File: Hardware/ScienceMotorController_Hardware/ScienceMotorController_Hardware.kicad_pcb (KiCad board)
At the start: 2 copper layers, 124.5 x 104.9 mm, 105 parts, among them SW1 SW_Push, SW2 SW_Push, SW3 SW_Push, SW4 SW_Push, SW5 SW_Push, U1 TM4C129E_Launchpad, U2 3.3V OKI, U3 5V OKI, U4 VNH5019A_E, U5 VNH5019A_E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

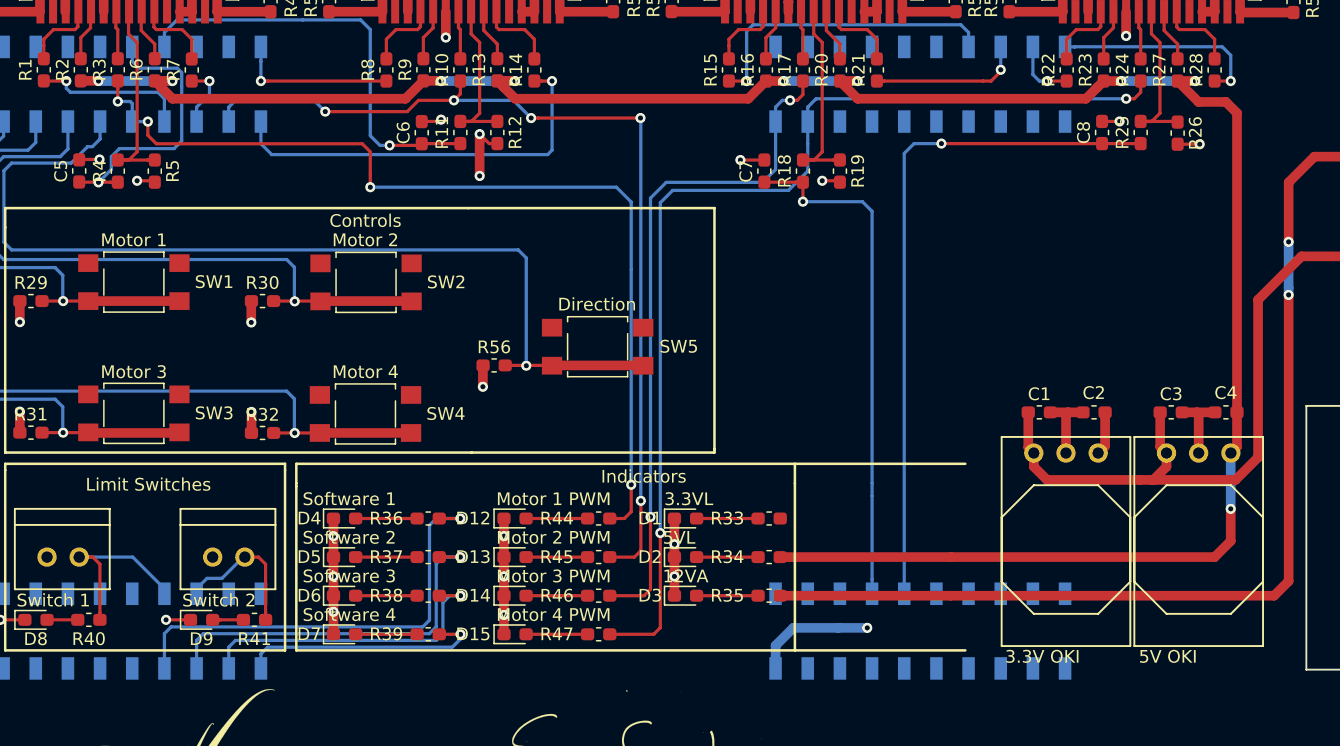
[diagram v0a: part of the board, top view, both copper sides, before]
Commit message: Similar to PostPDR, but using 3V3 instead of 5V for VNH5019A-E
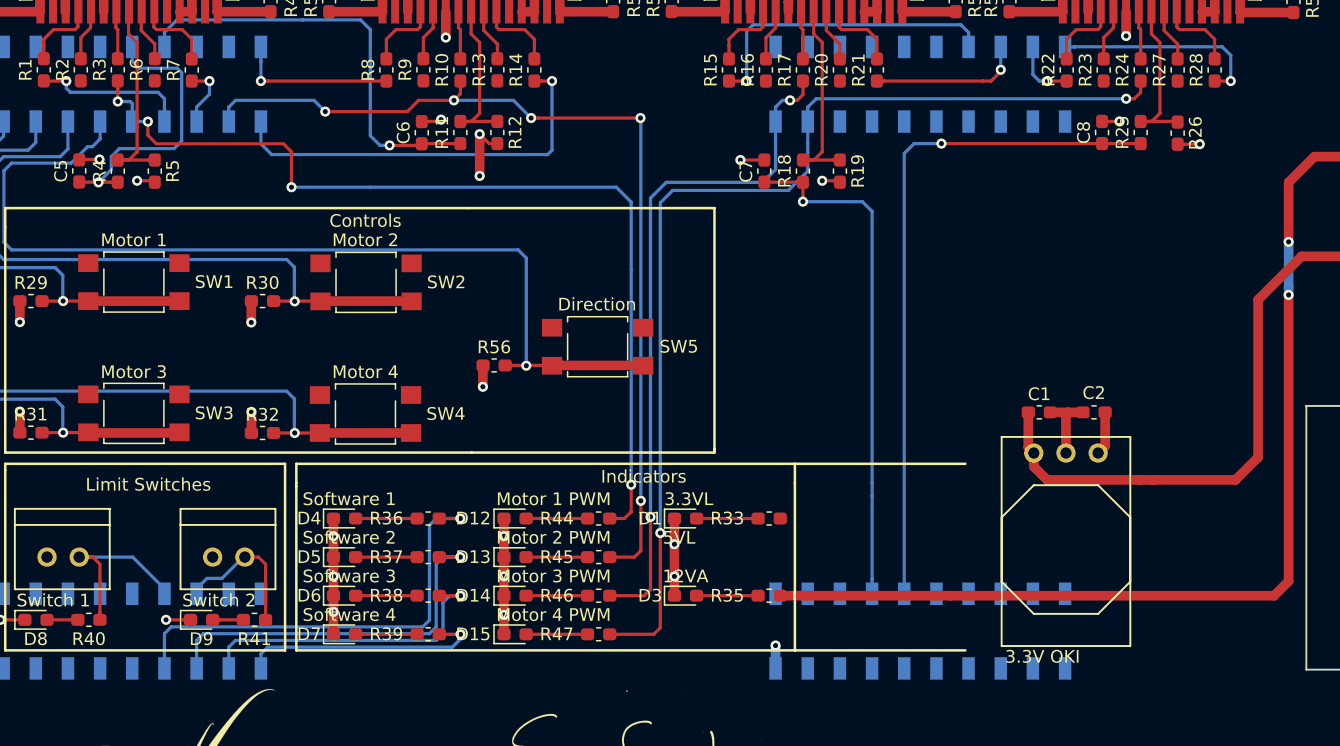
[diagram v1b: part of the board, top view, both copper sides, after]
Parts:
- removed C3, C4: 10uF, Capacitor_SMD:C_0603_1608Metric_Pad1.05x0.95mm_HandSolder
- removed D2: 5VL_LED, LED_SMD:LED_0603_1608Metric_Pad1.05x0.95mm_HandSolder
- removed R34: 500, Resistor_SMD:R_0603_1608Metric_Pad1.05x0.95mm_HandSolder
- removed U3: 5V OKI, MRDT_Devices:OKI_Horizontal
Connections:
- R13 pad 1: +5VL -> +3V3
- R16 pad 1: +5VL -> +3V3
- R2 pad 1: +5VL -> +3V3
- R20 pad 1: +5VL -> +3V3
- R23 pad 1: +5VL -> +3V3
- R27 pad 1: +5VL -> +3V3
- R6 pad 1: +5VL -> +3V3
- R9 pad 1: +5VL -> +3V3
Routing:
- net +5VL: track 182.7 -> 0.00 mm, vias 9 -> 0
- net +3V3: track 15.8 -> 7.95 mm
- net +12L: track 59.2 -> 53.2 mm
- net GND: track 188.5 -> 182.7 mm
- net Net-(D2-Pad2): track 4.85 -> 0.00 mm

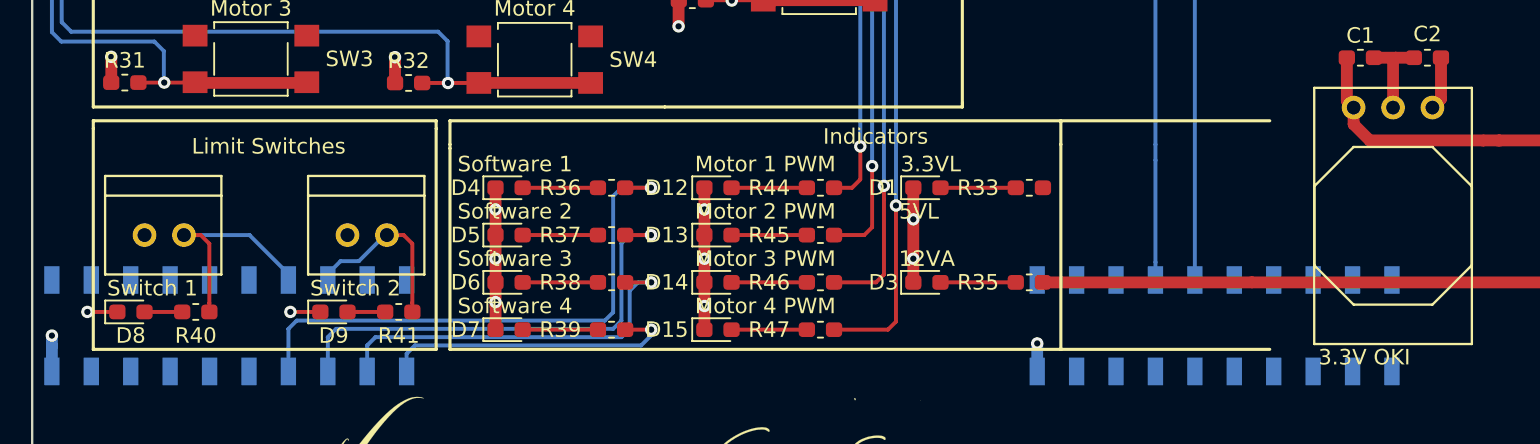
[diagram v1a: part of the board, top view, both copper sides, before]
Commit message: Added Pin Mapping
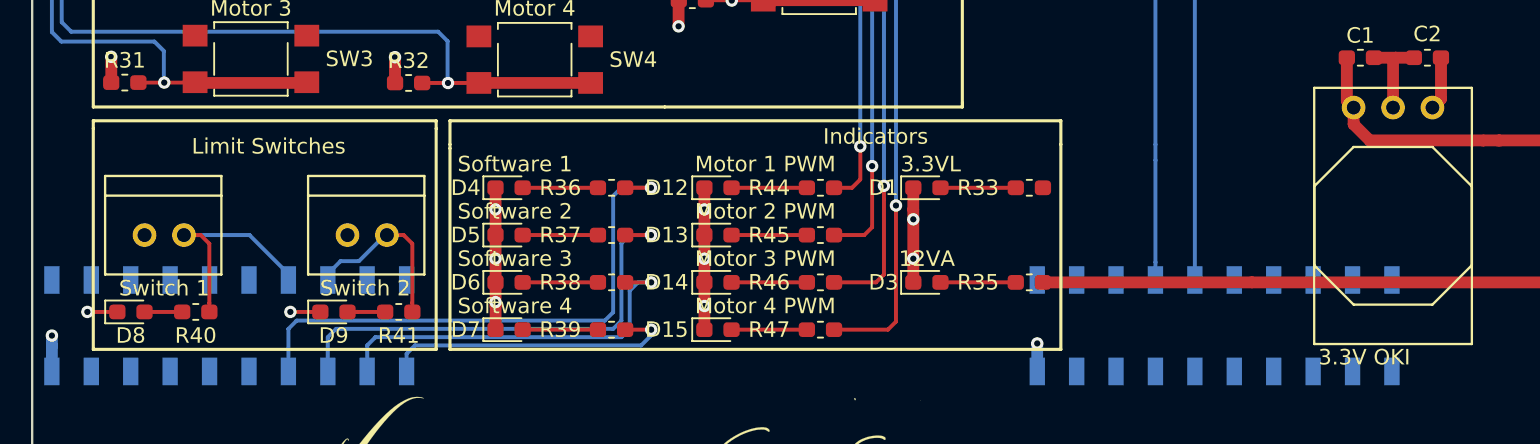
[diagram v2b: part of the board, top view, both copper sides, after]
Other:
- board text removed: "5VL"
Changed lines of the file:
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@@
   (general
     (thickness 1.6)
-    (drawings 71)
+    (drawings 70)
     (tracks 1149)
     (zones 0)
@@
     (38 B.Mask user)
     (39 F.Mask user)
-    (40 Dwgs.User user)
+    (40 Dwgs.User user hide)
     (41 Cmts.User user)
     (42 Eco1.User user)
@@
     (47 F.CrtYd user)
     (48 B.Fab user)
-    (49 F.Fab user)
+    (49 F.Fab user hide)
   )
   (setup
@@
     )
   )
+  (gr_line (start 104.902 123.698) (end 65.532 123.698) (layer F.SilkS) (width 0.2))
+  (gr_line (start 65.532 138.43) (end 104.902 138.43) (layer F.SilkS) (width 0.2))
   (gr_line (start 98.552 122.809) (end 98.552 122.555) (layer F.SilkS) (width 0.2))
   (gr_line (start 79.375 122.809) (end 98.552 122.809) (layer F.SilkS) (width 0.2))
@@
     (effects (font (size 1 1) (thickness 0.22206)))
   )
-  (gr_text "Switch 1" (at 46.355 134.493) (layer F.SilkS)
+  (gr_text "Switch 1" (at 47.117 134.493) (layer F.SilkS)
     (effects (font (size 1 1) (thickness 0.15)))
   )
-  (gr_text "Switch 2" (at 59.436 134.493) (layer F.SilkS)
+  (gr_text "Switch 2" (at 60.071 134.493) (layer F.SilkS)
     (effects (font (size 1 1) (thickness 0.15)))
   )
@@
     (effects (font (size 1 1) (thickness 0.15)))
   )
-  (gr_text 5VL (at 95.758 129.54) (layer F.SilkS)
-    (effects (font (size 1 1) (thickness 0.15)))
-  )
   (gr_text 3.3VL (at 96.52 126.492) (layer F.SilkS)
     (effects (font (size 1 1) (thickness 0.15)))
   )
   (gr_line (start 65.532 125.222) (end 65.532 125.476) (layer F.SilkS) (width 0.2))
-  (gr_line (start 118.364 123.698) (end 65.532 123.698) (layer F.SilkS) (width 0.2))
   (gr_line (start 104.902 138.43) (end 104.902 125.222) (layer F.SilkS) (width 0.2))
-  (gr_line (start 65.532 138.43) (end 118.364 138.43) (layer F.SilkS) (width 0.2))
   (gr_line (start 65.532 125.476) (end 65.532 138.43) (layer F.SilkS) (width 0.2))
   (gr_text "Science Motor Controller, Rev. 1, 2020\nMars Rover Design Team\nMissouri S&T\nAndrew Phillips, Sanfan Liu" (at 135.128 152.4) (layer F.SilkS)
@@
   (via (at 49.994291 99.664116) (size 0.8) (drill 0.4) (layers F.Cu B.Cu) (net 1))
   (segment (start 49.359291 99.664116) (end 49.994291 99.664116) (width 0.254) (layer F.Cu) (net 1))
-  (segment (start 123.331 122.4085) (end 123.7685 122.846) (width 0.762) (layer F.Cu) (net 2))
   (segment (start 123.331 119.634) (end 123.331 122.4085) (width 0.762) (layer F.Cu) (net 2))
   (segment (start 123.7685 123.92363) (end 124.81287 124.968) (width 0.762) (layer F.Cu) (net 2))
@@
   (segment (start 124.81287 124.968) (end 132.1265 124.968) (width 0.762) (layer F.Cu) (net 2))
   (segment (start 133.20413 124.968) (end 139.7 124.968) (width 0.762) (layer F.Cu) (net 2))
-  (segment (start 129.399 122.2955) (end 128.8485 122.846) (width 0.762) (layer F.Cu) (net 3))
+  (segment (start 123.7685 122.846) (end 123.331 122.4085) (width 0.762) (layer F.Cu) (net 2))
   (segment (start 129.399 119.634) (end 129.399 122.2955) (width 0.762) (layer F.Cu) (net 3))
   (segment (start 39.878 139.8524) (end 39.878 139.4587) (width 0.762) (layer B.Cu) (net 3))
@@
   (segment (start 103.378 138.049) (end 103.378 138.049) (width 0.762) (layer B.Cu) (net 3))
   (via (at 103.378 138.049) (size 0.8) (drill 0.4) (layers F.Cu B.Cu) (net 3))
+  (segment (start 128.8485 122.846) (end 129.399 122.2955) (width 0.762) (layer F.Cu) (net 3))
   (segment (start 50.86 101.459) (end 48.387 101.459) (width 0.254) (layer F.Cu) (net 4))
   (segment (start 51.435 101.459) (end 50.86 101.459) (width 0.254) (layer F.Cu) (net 4))
